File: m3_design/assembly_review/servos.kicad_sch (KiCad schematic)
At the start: 12 parts, among them J122 SERVO 3x4

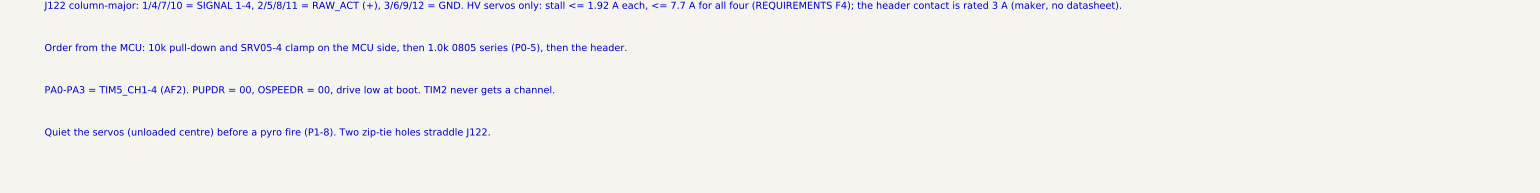
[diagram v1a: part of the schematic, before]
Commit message: M3-ASSY-R8: re-placed layout with planned-bus routing, owner-accepted deviations
R8 keeps R7's circuit, RF strip and CH1 pyro block (copied rigidly and
hash-asserted) and re-places everything else: U1 rotated so its free
pins face the RF strip, each block beside the U1 face it talks to, input
protection back at J1, and a fresh deterministic build (r8_build.sh)
with planned-bus routing, no autorouter and no patch stages.

Against R7: signal track 3.36 m -> 1.50 m, signal vias 217 -> 55,
simplicity index 100 -> 15.3, gate exceptions 74 -> 3, hard routing-rule
instances 10 -> 1, 7.7 A neck rise 38/30/44 -> 17.6/14.8/22.3 C,
unreferenced critical samples 27.9 % -> 11.1 %, non-pyro nets within
3 mm of armed copper 23 -> 7.

- Gate: check_r8 (pin contract from pin_table.tsv, F10 separation,
  battery/pyro clearance, loader-pin rule, rigid hashes), route_check
  profile r8, scorecard, dc_solve --necks, reference_audit, paste_check
- Review: passes 2, 3 and 4 found 0 Critical / 0 Major in all eight
  dimensions; pass 5 re-checked the final board (routing, planes,
  integrity) with 0 Critical / 0 Major
- Owner accepted the R8 deviation list on 2026-10-20, including the C10
  vibration item and the listed agent decisions

Board SHA-256 cc044ea0922ff826df19af9d9726d92c096ab2b127025b55d123d8772e5fb4a7.
tools/check.sh: DRC 0, unconnected 0, parity 0, ERC 0; audit, silk,
R8 contract, routing hygiene (0 failing, 3 allowlisted), actuator
contract and fit OK. Before ordering: consign U4, JLC tab acceptance,
cost/stock run within 24 h.

Co-Authored-By: Claude Opus 5.5 <noreply@anthropic.com>
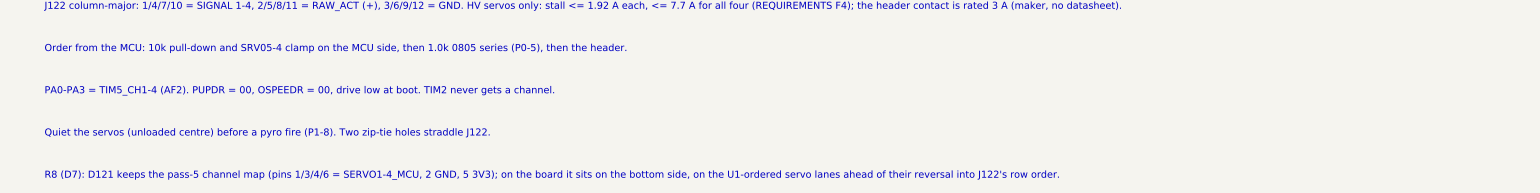
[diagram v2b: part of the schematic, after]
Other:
- note added: "R8 (D7): D121 keeps the pass-5 channel map (pins 1/3/4/6 = SERVO1-4_MCU, 2 GND, 5 3V3); on the board it sits on the bottom side, on the U1-ordered servo lanes ahead of their reversal into J122's row order."
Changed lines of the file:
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@@
 		(title "13 | Servo outputs")
 		(date "2026-09-25")
-		(rev "M3-ASSY-R7")
+		(rev "M3-ASSY-R8")
 		(company "Single-board M3 candidate; actuator merge, not bench-verified"))
 	(symbol
@@
 		(effects
 			(font
+				(size 1.27 1.27))
+			(justify left))
+)
+	(text "R8 (D7): D121 keeps the pass-5 channel map (pins 1/3/4/6 = SERVO1-4_MCU, 2 GND, 5 3V3); on the board it sits on the bottom side, on the U1-ordered servo lanes ahead of their reversal into J122's row order."
+		(at 20.32 275.48 0)
+		(effects
+			(font

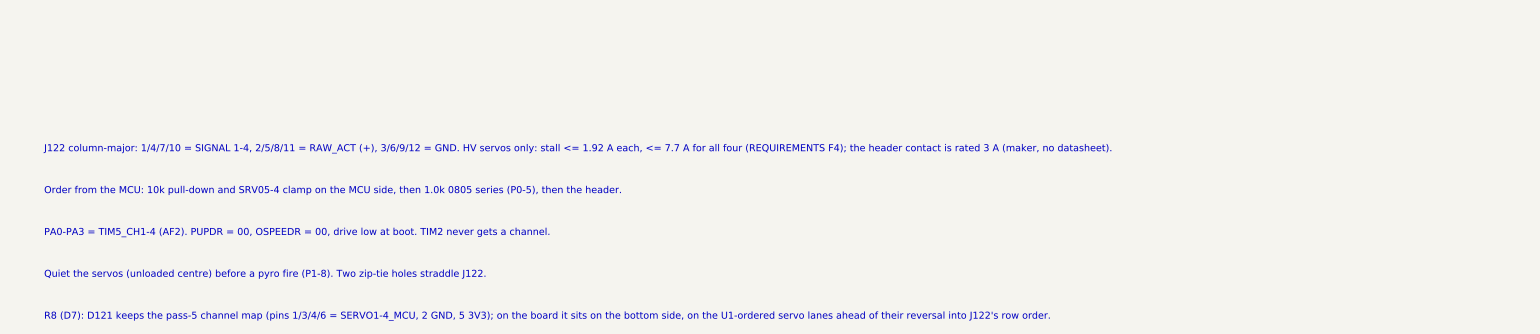
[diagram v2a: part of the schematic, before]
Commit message: M3-ASSY-R9: clean-sheet B-spine layout, 46 x 102 mm, owner-accepted deviations
R8's circuit laid out again from a clean sheet (r9_plan.md): the RF strip aft,
the CH1 pyro column as a dead end on the west edge, all power in the east
column. Built reproducibly from R8's sources by m3_design/r9_build.sh and
judged by the rule-based gate tools/check_r9.py; route_check profile r9 has an
empty allowlist and no leftovers. Every safety and RF qualification is
re-derived on the final board 4f841a0e (docs/R9_VALIDATION.md).

Review passes 1 and 2 found no confirmed Critical or Major; pass 1's Minors
were fixed through the generators, pass 2's 32 Minors are recorded. The owner
accepted the R9 deviation list on 2026-10-25, including the IMU turned 180
degrees (roll = -gyro_Y) and the crystal's local In2 GND plane, and kept the
board at 102 mm. tools/check.sh exits 0. R8 stays the accepted fallback.

Co-Authored-By: Claude Opus 5.5 <noreply@anthropic.com>
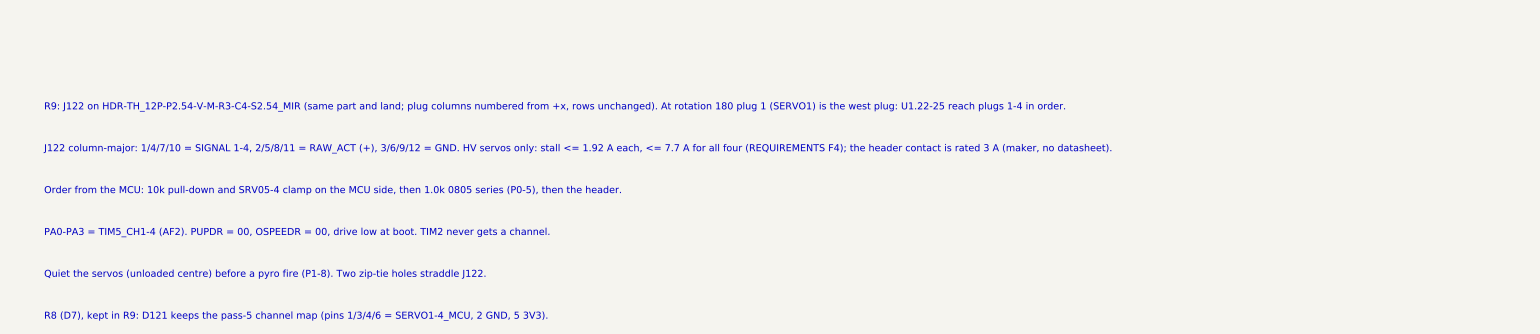
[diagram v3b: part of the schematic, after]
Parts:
- J122: footprint rocket:HDR-TH_12P-P2.54-V-M-R3-C4-S2.54 -> rocket:HDR-TH_12P-P2.54-V-M-R3-C4-S2.54_MIR
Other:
- note added: "R8 (D7), kept in R9: D121 keeps the pass-5 channel map (pins 1/3/4/6 = SERVO1-4_MCU, 2 GND, 5 3V3)."
- note added: "R9: J122 on HDR-TH_12P-P2.54-V-M-R3-C4-S2.54_MIR (same part and land; plug columns numbered from +x, rows unchanged). At rotation 180 plug 1 (SERVO1) is the west plug: U1.22-25 reach plugs 1-4 in order."
- note removed: "R8 (D7): D121 keeps the pass-5 channel map (pins 1/3/4/6 = SERVO1-4_MCU, 2 GND, 5 3V3); on the board it sits on the bottom side, on the U1-ordered servo lanes ahead of their reversal into J122's row order."
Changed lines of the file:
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@@
 		(title "13 | Servo outputs")
 		(date "2026-09-25")
-		(rev "M3-ASSY-R8")
+		(rev "M3-ASSY-R9")
 		(company "Single-board M3 candidate; actuator merge, not bench-verified"))
 	(symbol
@@
 					(size 1.27 1.27))
 				(justify left)))
-		(property "Footprint" "rocket:HDR-TH_12P-P2.54-V-M-R3-C4-S2.54"
+		(property "Footprint" "rocket:HDR-TH_12P-P2.54-V-M-R3-C4-S2.54_MIR"
 			(at 40.64 50.8 0)
 			(hide yes)
@@
 			(justify left))
 )
-	(text "R8 (D7): D121 keeps the pass-5 channel map (pins 1/3/4/6 = SERVO1-4_MCU, 2 GND, 5 3V3); on the board it sits on the bottom side, on the U1-ordered servo lanes ahead of their reversal into J122's row order."
+	(text "R8 (D7), kept in R9: D121 keeps the pass-5 channel map (pins 1/3/4/6 = SERVO1-4_MCU, 2 GND, 5 3V3)."
 		(at 20.32 275.48 0)
 		(effects
 			(font
+				(size 1.27 1.27))
+			(justify left))
+)
+	(text "R9: J122 on HDR-TH_12P-P2.54-V-M-R3-C4-S2.54_MIR (same part and land; plug columns numbered from +x, rows unchanged). At rotation 180 plug 1 (SERVO1) is the west plug: U1.22-25 reach plugs 1-4 in order."
+		(at 20.32 237.38 0)
+		(effects
+			(font
